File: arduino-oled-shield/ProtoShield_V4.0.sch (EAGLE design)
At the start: 22 parts

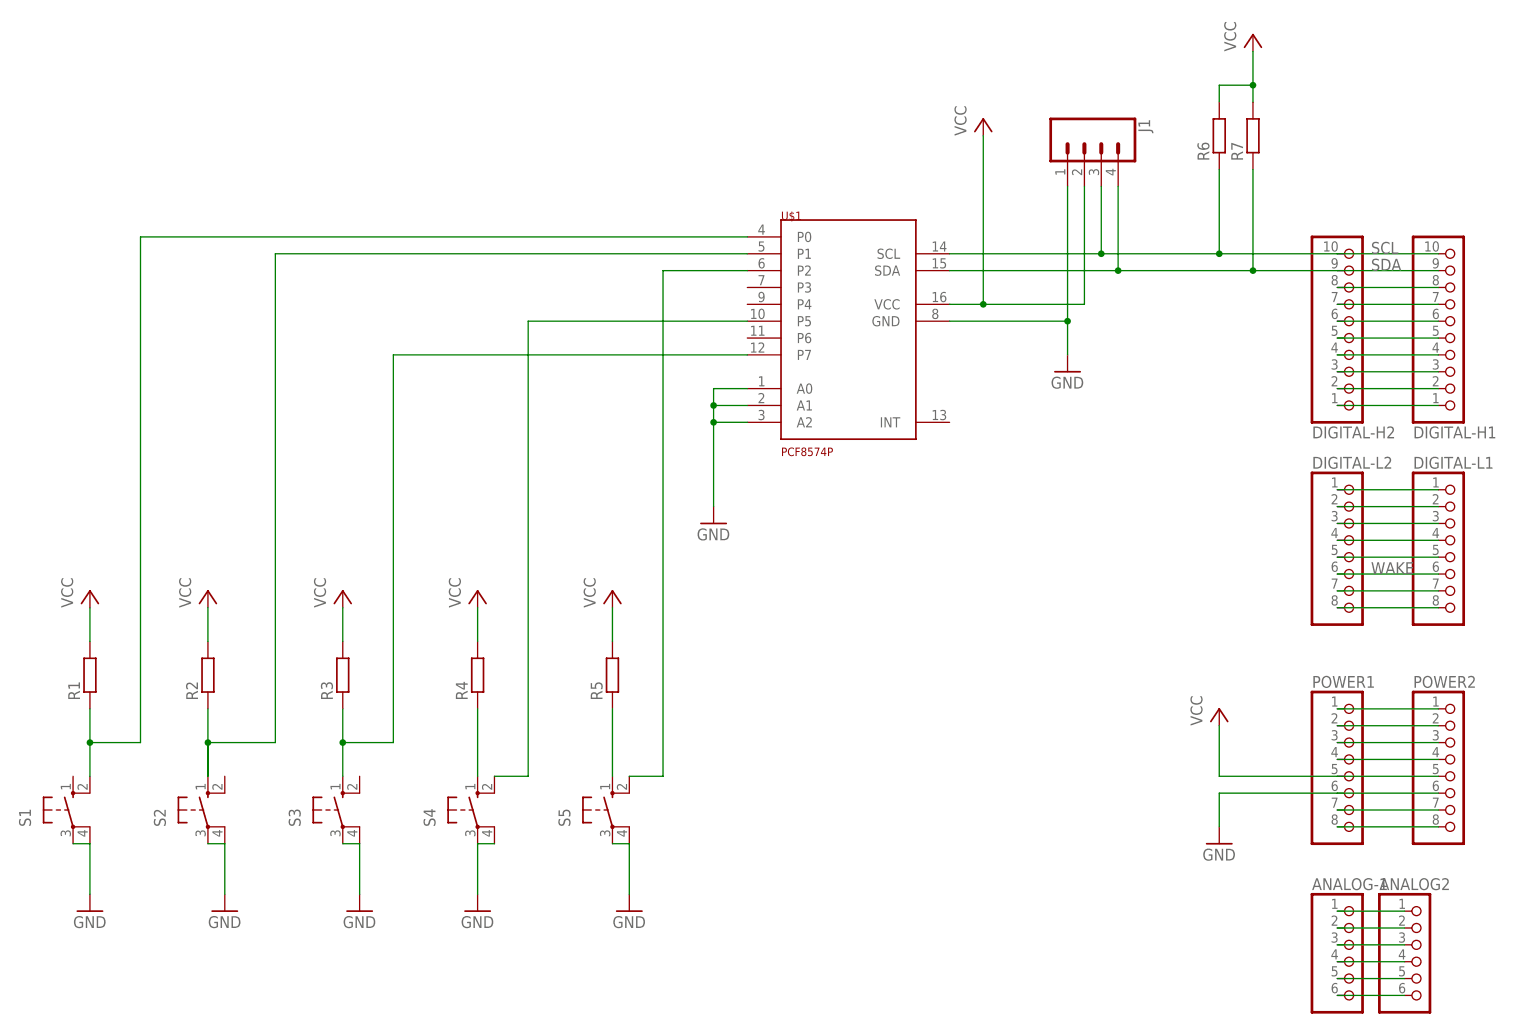
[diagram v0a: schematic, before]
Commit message: slow getButtonsNoneBlocking fixed, read analog only when used, popFromACC
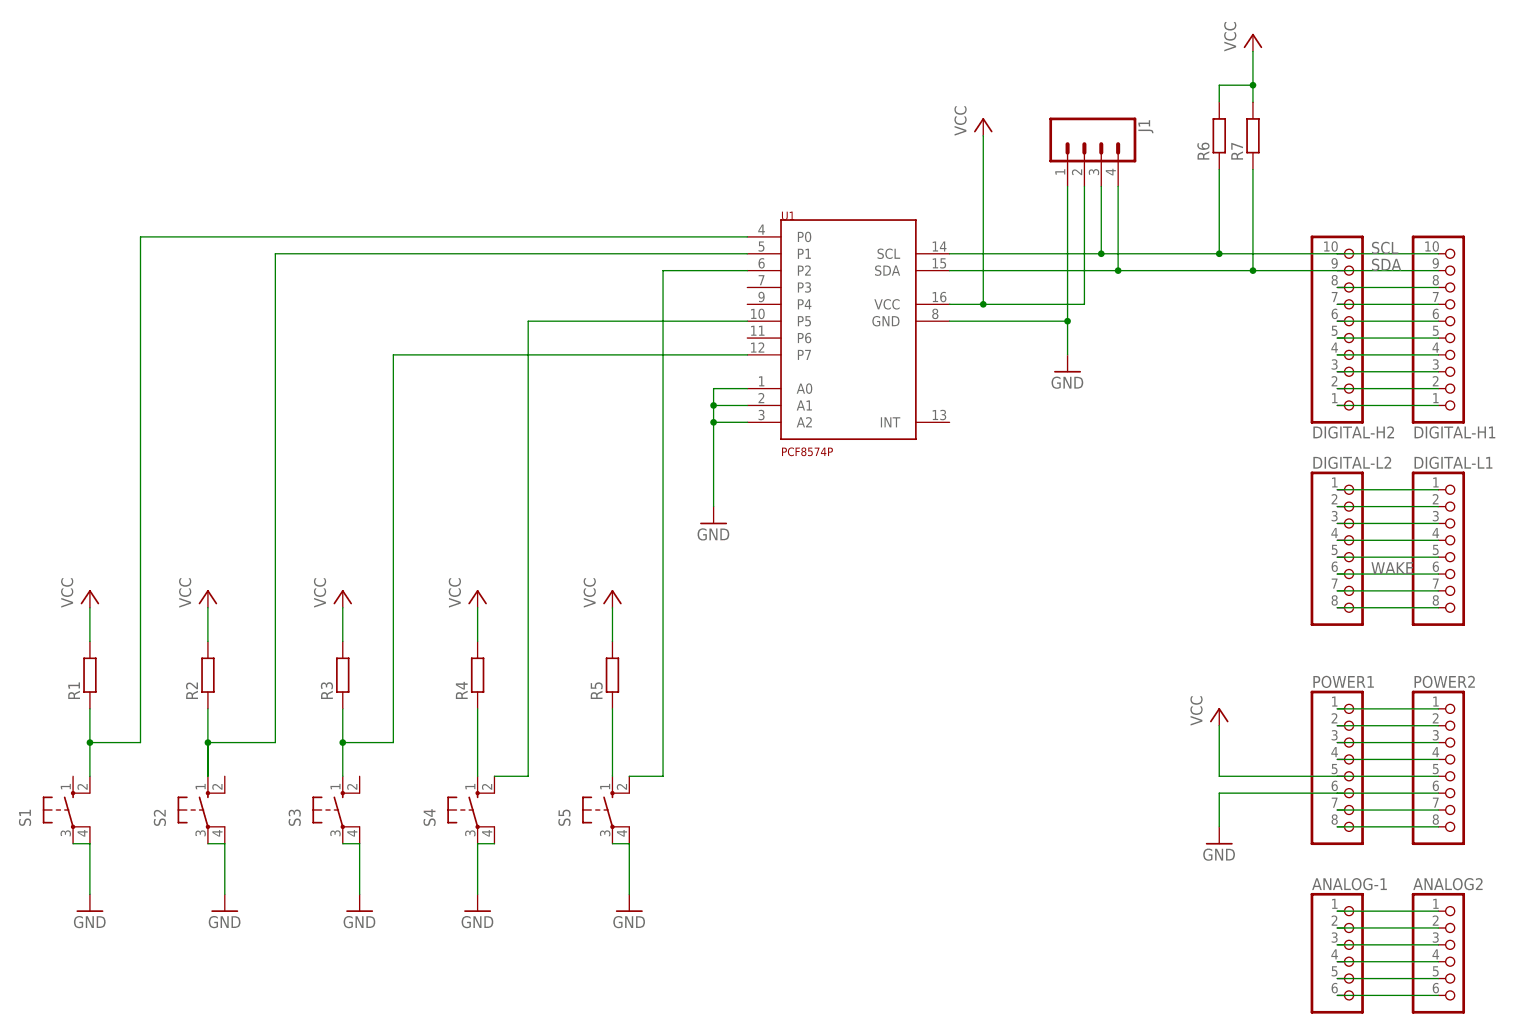
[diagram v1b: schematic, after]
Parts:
- renumbered U$1 to U1
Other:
- moved on the sheet: ANALOG2
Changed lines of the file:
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@@
 <attribute name="OC_FARNELL" value="unknown"/>
 </part>
-<part name="U$1" library="pcf8574p" deviceset="PCF8574P" device=""/>
+<part name="U1" library="pcf8574p" deviceset="PCF8574P" device=""/>
 <part name="S1" library="switch-omron" deviceset="10-XX" device=""/>
 <part name="S2" library="switch-omron" deviceset="10-XX" device=""/>
@@
 <attribute name="MPN" x="203.2" y="71.12" size="1.778" layer="96" display="off"/>
 </instance>
-<instance part="ANALOG2" gate="A" x="198.12" y="10.16">
-<attribute name="OC_FARNELL" x="198.12" y="10.16" size="1.778" layer="96" display="off"/>
-<attribute name="MF" x="198.12" y="10.16" size="1.778" layer="96" display="off"/>
-<attribute name="MPN" x="198.12" y="10.16" size="1.778" layer="96" display="off"/>
+<instance part="ANALOG2" gate="A" x="203.2" y="10.16">
+<attribute name="OC_FARNELL" x="203.2" y="10.16" size="1.778" layer="96" display="off"/>
+<attribute name="MF" x="203.2" y="10.16" size="1.778" layer="96" display="off"/>
+<attribute name="MPN" x="203.2" y="10.16" size="1.778" layer="96" display="off"/>
 </instance>
 <instance part="POWER2" gate="A" x="203.2" y="38.1">
@@
 <attribute name="MPN" x="187.96" y="38.1" size="1.778" layer="96" display="off"/>
 </instance>
-<instance part="U$1" gate="G$1" x="101.6" y="121.92"/>
+<instance part="U1" gate="G$1" x="101.6" y="121.92"/>
 <instance part="S1" gate="1" x="-5.08" y="33.02"/>
 <instance part="S2" gate="1" x="15.24" y="33.02"/>
@@
 <net name="N$18" class="0">
 <segment>
-<wire x1="195.58" y1="17.78" x2="185.42" y2="17.78" width="0.1524" layer="91"/>
+<wire x1="200.66" y1="17.78" x2="185.42" y2="17.78" width="0.1524" layer="91"/>
 <pinref part="ANALOG-1" gate="A" pin="1"/>
 <pinref part="ANALOG2" gate="A" pin="1"/>
@@
 <net name="N$19" class="0">
 <segment>
-<wire x1="195.58" y1="15.24" x2="185.42" y2="15.24" width="0.1524" layer="91"/>
+<wire x1="200.66" y1="15.24" x2="185.42" y2="15.24" width="0.1524" layer="91"/>
 <pinref part="ANALOG-1" gate="A" pin="2"/>
 <pinref part="ANALOG2" gate="A" pin="2"/>
@@
 <net name="N$20" class="0">
 <segment>
-<wire x1="195.58" y1="12.7" x2="185.42" y2="12.7" width="0.1524" layer="91"/>
+<wire x1="200.66" y1="12.7" x2="185.42" y2="12.7" width="0.1524" layer="91"/>
 <pinref part="ANALOG-1" gate="A" pin="3"/>
 <pinref part="ANALOG2" gate="A" pin="3"/>
@@
 <net name="N$21" class="0">
 <segment>
-<wire x1="195.58" y1="10.16" x2="185.42" y2="10.16" width="0.1524" layer="91"/>
+<wire x1="200.66" y1="10.16" x2="185.42" y2="10.16" width="0.1524" layer="91"/>
 <pinref part="ANALOG-1" gate="A" pin="4"/>
 <pinref part="ANALOG2" gate="A" pin="4"/>
@@
 <net name="N$22" class="0">
 <segment>
-<wire x1="195.58" y1="7.62" x2="185.42" y2="7.62" width="0.1524" layer="91"/>
+<wire x1="200.66" y1="7.62" x2="185.42" y2="7.62" width="0.1524" layer="91"/>
 <pinref part="ANALOG-1" gate="A" pin="5"/>
 <pinref part="ANALOG2" gate="A" pin="5"/>
@@
 <net name="N$23" class="0">
 <segment>
-<wire x1="195.58" y1="5.08" x2="185.42" y2="5.08" width="0.1524" layer="91"/>
+<wire x1="200.66" y1="5.08" x2="185.42" y2="5.08" width="0.1524" layer="91"/>
 <pinref part="ANALOG-1" gate="A" pin="6"/>
 <pinref part="ANALOG2" gate="A" pin="6"/>
@@
 <pinref part="DIGITAL-H1" gate="A" pin="9"/>
 <label x="190.5" y="114.3" size="1.778" layer="95"/>
-<pinref part="U$1" gate="G$1" pin="SDA"/>
+<pinref part="U1" gate="G$1" pin="SDA"/>
 <wire x1="127" y1="114.3" x2="152.4" y2="114.3" width="0.1524" layer="91"/>
 <pinref part="R7" gate="G$1" pin="1"/>
@@
 <pinref part="DIGITAL-H1" gate="A" pin="10"/>
 <label x="190.5" y="116.84" size="1.778" layer="95"/>
-<pinref part="U$1" gate="G$1" pin="SCL"/>
+<pinref part="U1" gate="G$1" pin="SCL"/>
 <wire x1="127" y1="116.84" x2="149.86" y2="116.84" width="0.1524" layer="91"/>
 <pinref part="R6" gate="G$1" pin="1"/>
@@
 <pinref part="R1" gate="G$1" pin="1"/>
 <wire x1="-2.54" y1="38.1" x2="-2.54" y2="43.18" width="0.1524" layer="91"/>
-<pinref part="U$1" gate="G$1" pin="P0"/>
+<pinref part="U1" gate="G$1" pin="P0"/>
 <wire x1="-2.54" y1="43.18" x2="-2.54" y2="48.26" width="0.1524" layer="91"/>
 <wire x1="96.52" y1="119.38" x2="5.08" y2="119.38" width="0.1524" layer="91"/>
@@
 <pinref part="R3" gate="G$1" pin="1"/>
 <wire x1="35.56" y1="38.1" x2="35.56" y2="43.18" width="0.1524" layer="91"/>
-<pinref part="U$1" gate="G$1" pin="P7"/>
+<pinref part="U1" gate="G$1" pin="P7"/>
 <wire x1="35.56" y1="43.18" x2="35.56" y2="48.26" width="0.1524" layer="91"/>
 <wire x1="96.52" y1="101.6" x2="43.18" y2="101.6" width="0.1524" layer="91"/>
@@
 <net name="N$37" class="0">
 <segment>
-<pinref part="U$1" gate="G$1" pin="P2"/>
+<pinref part="U1" gate="G$1" pin="P2"/>
 <wire x1="96.52" y1="114.3" x2="83.82" y2="114.3" width="0.1524" layer="91"/>
 <wire x1="83.82" y1="114.3" x2="83.82" y2="38.1" width="0.1524" layer="91"/>
@@
 <net name="N$33" class="0">
 <segment>
-<pinref part="U$1" gate="G$1" pin="P5"/>
+<pinref part="U1" gate="G$1" pin="P5"/>
 <wire x1="96.52" y1="106.68" x2="63.5" y2="106.68" width="0.1524" layer="91"/>
 <wire x1="63.5" y1="106.68" x2="63.5" y2="38.1" width="0.1524" layer="91"/>
@@
 </segment>
 <segment>
-<pinref part="U$1" gate="G$1" pin="A0"/>
+<pinref part="U1" gate="G$1" pin="A0"/>
 <wire x1="96.52" y1="96.52" x2="91.44" y2="96.52" width="0.1524" layer="91"/>
 <wire x1="91.44" y1="96.52" x2="91.44" y2="93.98" width="0.1524" layer="91"/>
-<pinref part="U$1" gate="G$1" pin="A1"/>
+<pinref part="U1" gate="G$1" pin="A1"/>
 <wire x1="91.44" y1="93.98" x2="91.44" y2="91.44" width="0.1524" layer="91"/>
 <wire x1="91.44" y1="91.44" x2="91.44" y2="78.74" width="0.1524" layer="91"/>
 <wire x1="96.52" y1="93.98" x2="91.44" y2="93.98" width="0.1524" layer="91"/>
-<pinref part="U$1" gate="G$1" pin="A2"/>
+<pinref part="U1" gate="G$1" pin="A2"/>
 <wire x1="96.52" y1="91.44" x2="91.44" y2="91.44" width="0.1524" layer="91"/>
 <junction x="91.44" y="93.98"/>
@@
 </segment>
 <segment>
-<pinref part="U$1" gate="G$1" pin="GND"/>
+<pinref part="U1" gate="G$1" pin="GND"/>
 <pinref part="GND7" gate="1" pin="GND"/>
 <wire x1="127" y1="106.68" x2="144.78" y2="106.68" width="0.1524" layer="91"/>
@@
 <segment>
 <pinref part="P+6" gate="VCC" pin="VCC"/>
-<pinref part="U$1" gate="G$1" pin="VCC"/>
+<pinref part="U1" gate="G$1" pin="VCC"/>
 <wire x1="127" y1="109.22" x2="132.08" y2="109.22" width="0.1524" layer="91"/>
 <wire x1="132.08" y1="109.22" x2="132.08" y2="134.62" width="0.1524" layer="91"/>
@@
 <net name="N$5" class="0">
 <segment>
-<pinref part="U$1" gate="G$1" pin="P1"/>
+<pinref part="U1" gate="G$1" pin="P1"/>
 <wire x1="96.52" y1="116.84" x2="25.4" y2="116.84" width="0.1524" layer="91"/>
 <wire x1="25.4" y1="116.84" x2="25.4" y2="43.18" width="0.1524" layer="91"/>
